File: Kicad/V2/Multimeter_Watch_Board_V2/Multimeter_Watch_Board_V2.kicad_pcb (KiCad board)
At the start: 4 copper layers, 46 x 42 mm, 51 parts, among them J1 S3B-PH-K-S(LF)(SN), J2 S3B-PH-K-S(LF)(SN), J3 S3B-PH-K-S(LF)(SN), J6 51281-1294, J7 Conn_01x11_Female, J8 Conn_01x11_Female, Q1 A03400A N-MOS, U1 PCF85163-SO08, U2 AD8592, Y1 32kHz

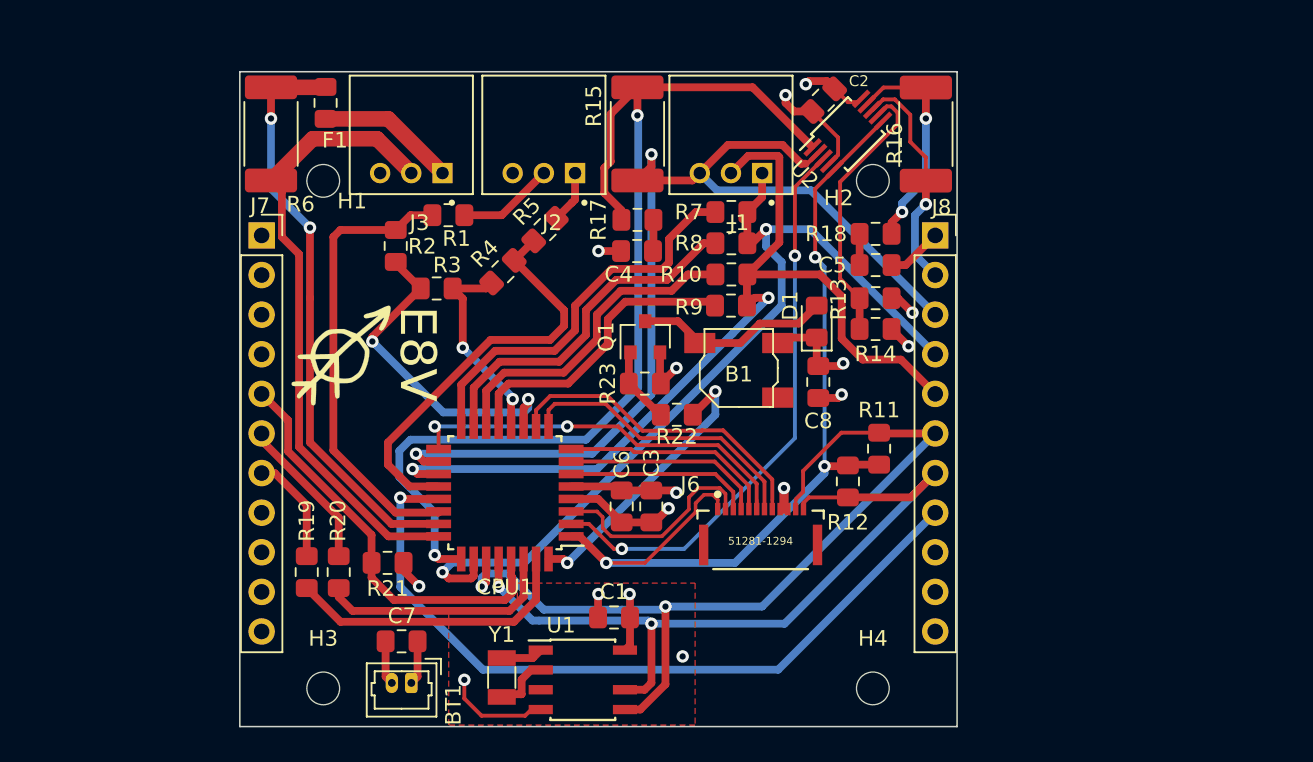
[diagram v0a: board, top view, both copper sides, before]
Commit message: females layout improvements, add silkscreen labels for female pins
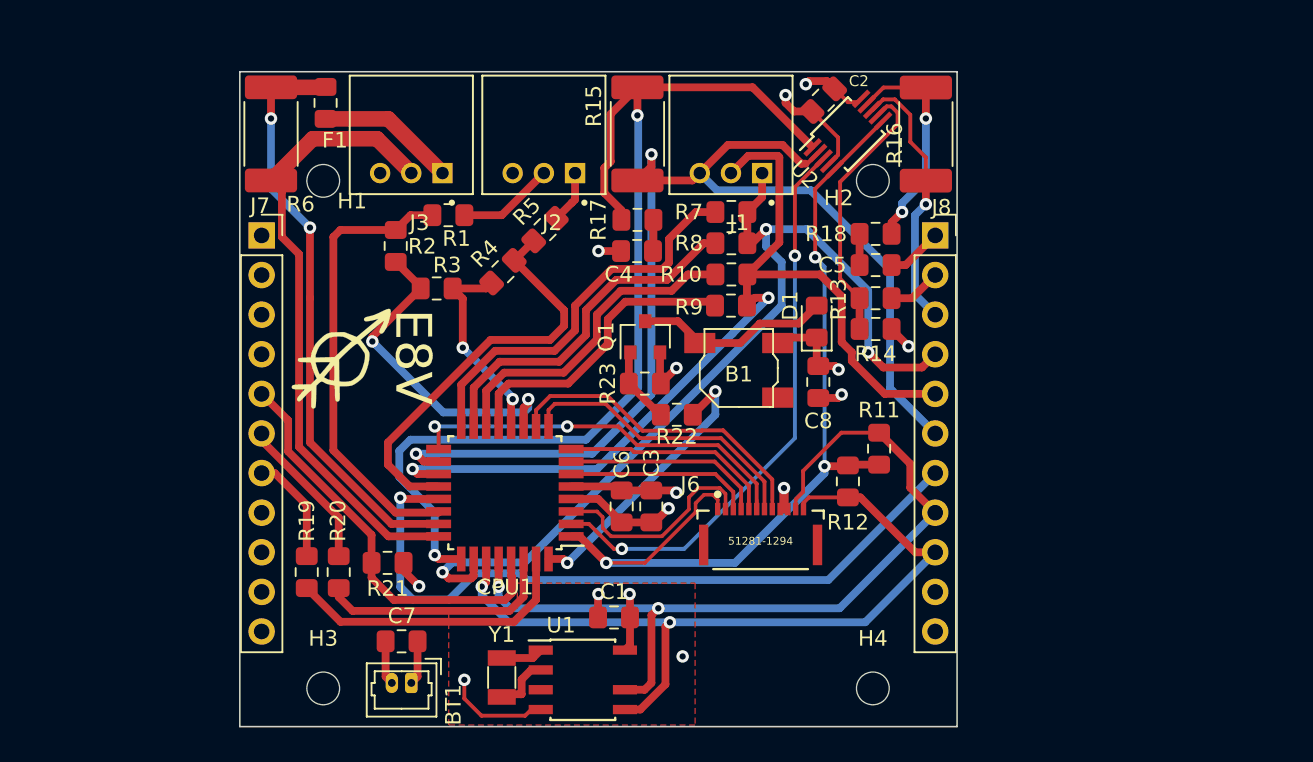
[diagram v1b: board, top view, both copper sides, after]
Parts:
- added G***: LOGO, Multimeter_Watch_Custom_Footprints:github_logo, B.Cu at (135.2, 66.8)
- moved G*** 0.20 mm to (108.5, 76.4)
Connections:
- J8 pad 2: /VCC_HALF -> /VCC
- J8 pad 3: /DACout -> /VCC_HALF
- J8 pad 6: /SCL -> /DACout
- J8 pad 7: /SDA -> /SWD
- J8 pad 8: /SWD -> /SCL
- J8 pad 9: Net-(J8-Pad9) -> /SDA
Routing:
- net /DACout: track 69.1 -> 76.9 mm
- net /SDA: track 55.2 -> 51.9 mm
- net /ADC3: track 58.1 -> 61.2 mm, vias 2 -> 3
- net /SCL: track 52.6 -> 55.4 mm
- net /VCC_HALF: track 14.7 -> 17.2 mm
- net /SWD: track 48.9 -> 46.6 mm
- net /VCC: track 27.9 -> 29.3 mm, vias 6 -> 5
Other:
- board text added: ":ptrbroz/Multimeter_watch"
- board text added: "ADC3"
- board text added: "ADC6"
- board text added: "D0"
- board text added: "D1"
- board text added: "DAC/SWC"
- board text added: "GND"
- board text added: "RESET"
- board text added: "SCL"
- board text added: "SDA"
- board text added: "SWD"
- board text added: "VCC"
- board text added: "VCC/2"

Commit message: top board rework (move flex conn up, dedicated display enable)
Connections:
- J6 pad 1: /PD3 -> /VCC
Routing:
- net /PD3: track 57.6 -> 47.5 mm
- net /VCC: track 29.3 -> 32.5 mm, vias 5 -> 6

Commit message: add rlc tester protection to schematic
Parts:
- added D2: D, Multimeter_Watch_Custom_Footprints:1408D, F.Cu at (157.0, 73.0)
- added D3: D, Multimeter_Watch_Custom_Footprints:1408D, F.Cu at (157.0, 76.5)
- added D4: D, Multimeter_Watch_Custom_Footprints:1408D, F.Cu at (162.0, 73.0)
- added D5: D, Multimeter_Watch_Custom_Footprints:1408D, F.Cu at (162.0, 76.5)
- added D6: D, Multimeter_Watch_Custom_Footprints:1408D, F.Cu at (166.9, 73.0)
- added D7: D, Multimeter_Watch_Custom_Footprints:1408D, F.Cu at (166.9, 76.5)
- added F2: Fuse, Fuse:Fuse_0805_2012Metric_Pad1.15x1.40mm_HandSolder, F.Cu at (156.8, 79.8)
- added F3: Fuse, Fuse:Fuse_0805_2012Metric_Pad1.15x1.40mm_HandSolder, F.Cu at (161.6, 79.8)
- added F4: Fuse, Fuse:Fuse_0805_2012Metric_Pad1.15x1.40mm_HandSolder, F.Cu at (166.3, 79.8)
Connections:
- J1 pad 1: /ADC3 -> Net-(F2-Pad2)
- J1 pad 2: /ADC6 -> Net-(F3-Pad2)
- J1 pad 3: /DACout -> Net-(F4-Pad1)
- R19 pad 1: Net-(CPU1-Pad31) -> /D1
- R19 pad 2: /D1 -> Net-(CPU1-Pad31)
- R20 pad 1: Net-(CPU1-Pad30) -> /D0
- R20 pad 2: /D0 -> Net-(CPU1-Pad30)

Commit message: implement rlc protection (likely to be reverted)
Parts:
- moved D7 41.8 mm to (125.6, 70.0), turned to 180 degrees
- moved D6 41.7 mm to (125.6, 67.5)
- moved F4 39.2 mm to (128.9, 68.2), turned to 270 degrees
- moved D5 38.9 mm to (123.2, 73.4), turned to 90 degrees
- moved D4 36.3 mm to (125.8, 75.6), turned to 90 degrees
- moved F3 34.7 mm to (127.7, 72.3)
- moved C8 29.7 mm to (117.0, 97.7), turned to 90 degrees
- moved Y1 28.5 mm to (137.4, 75.2), turned to 225 degrees
- moved F2 26.2 mm to (133.4, 67.9), turned to 90 degrees
- moved D3 25.4 mm to (131.9, 72.5), turned to 180 degrees
- moved D1 25.4 mm to (127.1, 96.4), turned to 0 degrees
- moved D2 25.2 mm to (131.9, 75.1)
- moved B1 23.6 mm to (121.9, 97.3), turned to 0 degrees
- moved U1 23.5 mm to (140.5, 80.2), turned to 315 degrees
- moved C1 23.5 mm to (143.5, 77.3), turned to 315 degrees
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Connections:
- F2 pad 2: Net-(F2-Pad2) -> /RLC1
- F3 pad 2: Net-(F3-Pad2) -> /RLC2
- F4 pad 1: Net-(F4-Pad1) -> /RLC3
- J1 pad 1: Net-(F2-Pad2) -> /RLC1
- J1 pad 2: Net-(F3-Pad2) -> /RLC2
- J1 pad 3: Net-(F4-Pad1) -> /RLC3
- J3 pad 2: /ADC1 -> Net-(J3-Pad2)
- J3 pad 3: Net-(J3-Pad3) -> /ADC1
- J8 pad 2: /VCC -> /VCC_HALF
- J8 pad 3: /VCC_HALF -> /DACout
- J8 pad 4: /ADC3 -> /RLC1
- J8 pad 5: /ADC6 -> /RLC2
- J8 pad 6: /DACout -> /RLC3
- R1 pad 1: Net-(J2-Pad2) -> Net-(J2-Pad3)
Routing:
- net /ADC6: track 62.0 -> 28.3 mm
- net /RLC2: track 0.00 -> 30.8 mm
- net /RLC3: track 0.00 -> 28.4 mm
- net /ADC3: track 61.2 -> 38.6 mm, vias 3 -> 2
- net /RLC1: track 0.00 -> 20.3 mm
- net /VCC: track 32.5 -> 50.7 mm, vias 6 -> 7
- net /PD2: track 18.3 -> 2.36 mm, vias 2 -> 0
- net /PB1: track 19.5 -> 4.51 mm
- net /PB2: track 21.0 -> 6.93 mm
- net /PD7: track 21.6 -> 32.2 mm
- net /PB0: track 13.1 -> 23.6 mm
- net /ADC10: track 26.9 -> 16.7 mm
- net Net-(J2-Pad3): track 0.00 -> 8.16 mm
- net /DACout: track 76.9 -> 69.6 mm, vias 2 -> 3
- net /GND: track 38.2 -> 45.5 mm, vias 10 -> 9
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
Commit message: Revert "implement rlc protection (likely to be reverted)"
This reverts commit 3bbffdcc62f9ba327af4a0488dca8880d003efb7.
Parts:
- moved D7 41.8 mm to (166.9, 76.5), turned to 0 degrees
- moved D6 41.7 mm to (166.9, 73.0)
- moved F4 39.2 mm to (166.3, 79.8), turned to 0 degrees
- moved D5 38.9 mm to (162.0, 76.5), turned to 0 degrees
- moved D4 36.3 mm to (162.0, 73.0), turned to 0 degrees
- moved F3 34.7 mm to (161.6, 79.8)
- moved C8 29.7 mm to (139.1, 77.9), turned to 270 degrees
- moved Y1 28.5 mm to (118.8, 96.8), turned to 270 degrees
- moved F2 26.2 mm to (156.8, 79.8), turned to 0 degrees
- moved D3 25.4 mm to (157.0, 76.5), turned to 0 degrees
- moved D1 25.4 mm to (139.0, 74.0), turned to 90 degrees
- moved D2 25.2 mm to (157.0, 73.0)
- moved B1 23.6 mm to (134.0, 77.0), turned to 180 degrees
- moved U1 23.5 mm to (124.0, 97.0), turned to 0 degrees
- moved C1 23.5 mm to (126.0, 93.0), turned to 0 degrees
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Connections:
- F2 pad 2: /RLC1 -> Net-(F2-Pad2)
- F3 pad 2: /RLC2 -> Net-(F3-Pad2)
- F4 pad 1: /RLC3 -> Net-(F4-Pad1)
- J1 pad 1: /RLC1 -> Net-(F2-Pad2)
- J1 pad 2: /RLC2 -> Net-(F3-Pad2)
- J1 pad 3: /RLC3 -> Net-(F4-Pad1)
- J3 pad 2: Net-(J3-Pad2) -> /ADC1
- J3 pad 3: /ADC1 -> Net-(J3-Pad3)
- J8 pad 2: /VCC_HALF -> /VCC
- J8 pad 3: /DACout -> /VCC_HALF
- J8 pad 4: /RLC1 -> /ADC3
- J8 pad 5: /RLC2 -> /ADC6
- J8 pad 6: /RLC3 -> /DACout
- R1 pad 1: Net-(J2-Pad3) -> Net-(J2-Pad2)
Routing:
- net /ADC6: track 28.3 -> 62.0 mm
- net /RLC2: track 30.8 -> 0.00 mm
- net /RLC3: track 28.4 -> 0.00 mm
- net /ADC3: track 38.6 -> 61.2 mm, vias 2 -> 3
- net /RLC1: track 20.3 -> 0.00 mm
- net /VCC: track 50.7 -> 32.5 mm, vias 7 -> 6
- net /PD2: track 2.36 -> 18.3 mm, vias 0 -> 2
- net /PB1: track 4.51 -> 19.5 mm
- net /PB2: track 6.93 -> 21.0 mm
- net /PD7: track 32.2 -> 21.6 mm
- net /PB0: track 23.6 -> 13.1 mm
- net /ADC10: track 16.7 -> 26.9 mm
- net Net-(J2-Pad3): track 8.16 -> 0.00 mm
- net /DACout: track 69.6 -> 76.9 mm, vias 3 -> 2
- net /GND: track 45.5 -> 38.2 mm, vias 9 -> 10
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
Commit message: Revert "add rlc tester protection to schematic"
This reverts commit df46bc8d5560e11f4e55d6f466ca62c966db9fe4.
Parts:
- removed D2, D3, D4, D5, D6, D7: D, Multimeter_Watch_Custom_Footprints:1408D
- removed F2, F3, F4: Fuse, Fuse:Fuse_0805_2012Metric_Pad1.15x1.40mm_HandSolder
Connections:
- J1 pad 1: Net-(F2-Pad2) -> /ADC3
- J1 pad 2: Net-(F3-Pad2) -> /ADC6
- J1 pad 3: Net-(F4-Pad1) -> /DACout
- R19 pad 1: /D1 -> Net-(CPU1-Pad31)
- R19 pad 2: Net-(CPU1-Pad31) -> /D1
- R20 pad 1: /D0 -> Net-(CPU1-Pad30)
- R20 pad 2: Net-(CPU1-Pad30) -> /D0
